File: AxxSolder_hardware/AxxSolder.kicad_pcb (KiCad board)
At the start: 2 copper layers, 39 x 82.5 mm, 138 parts, among them IC1 TLV76733DRVR, IC2 OPA2387DSGT, IC3 LMR54406DBVR, IC4 STM32G431CBT6, IC5 TPD4E1U06DBVR, IC6 STUSB4500QTR, IC7 MAX16171ATA_VY+T, IC8 LTC4440AHMS8E, IC9 INA281A5QDBVRQ1, J1 USB4110-GF-A, J2 691243110009, J3 TSW-102-07-T-S, J4 61300611821, J5 TSW-102-07-T-S, J6 TSW-102-07-T-S, Q1 STL9P3LLH6, Q2 STL10N3LLH5, Q3 2N7002NXAKR, U2 PEC11J-9215F-S0015, U3 BSC014N04LS

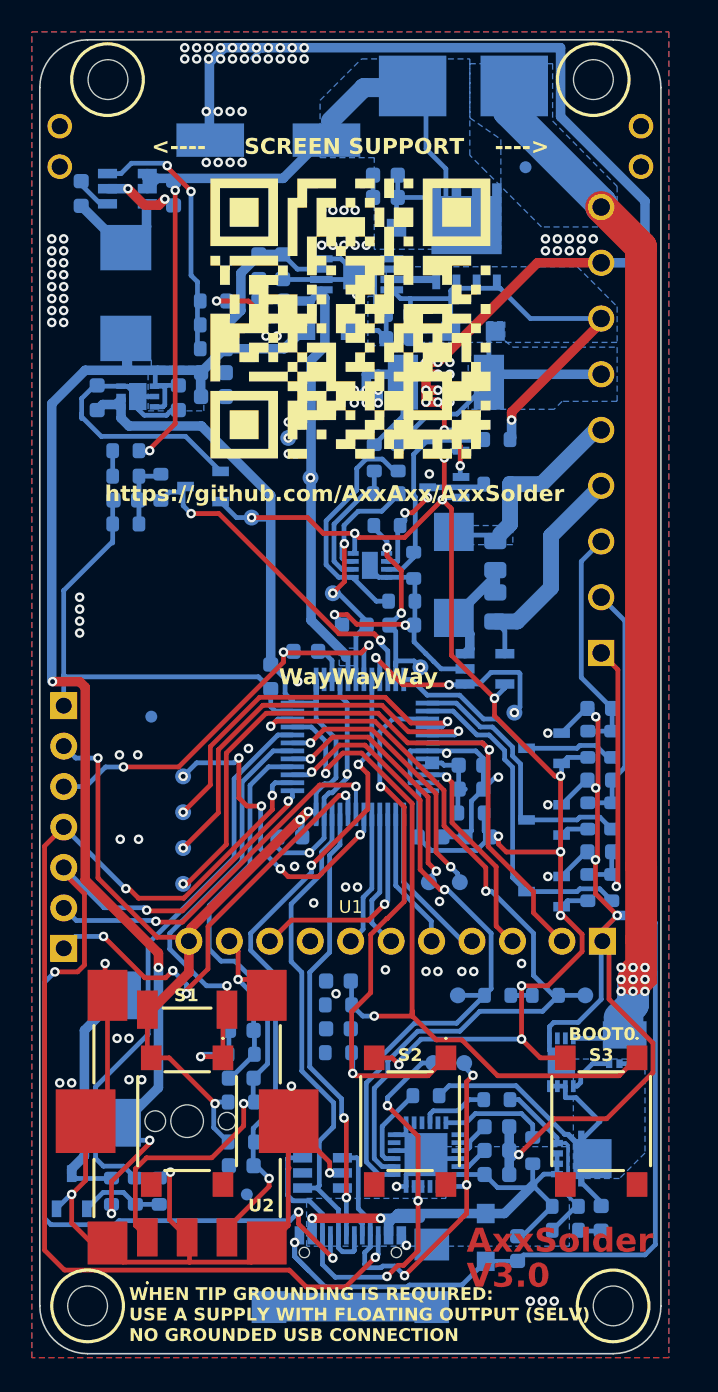
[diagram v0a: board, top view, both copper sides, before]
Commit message: Create Lite version of board
Mark all USB-C components as DNP (except I2C pullups)
Swap LCD footprint from Adafruit 4311 to commodity GMT020-02 LCD
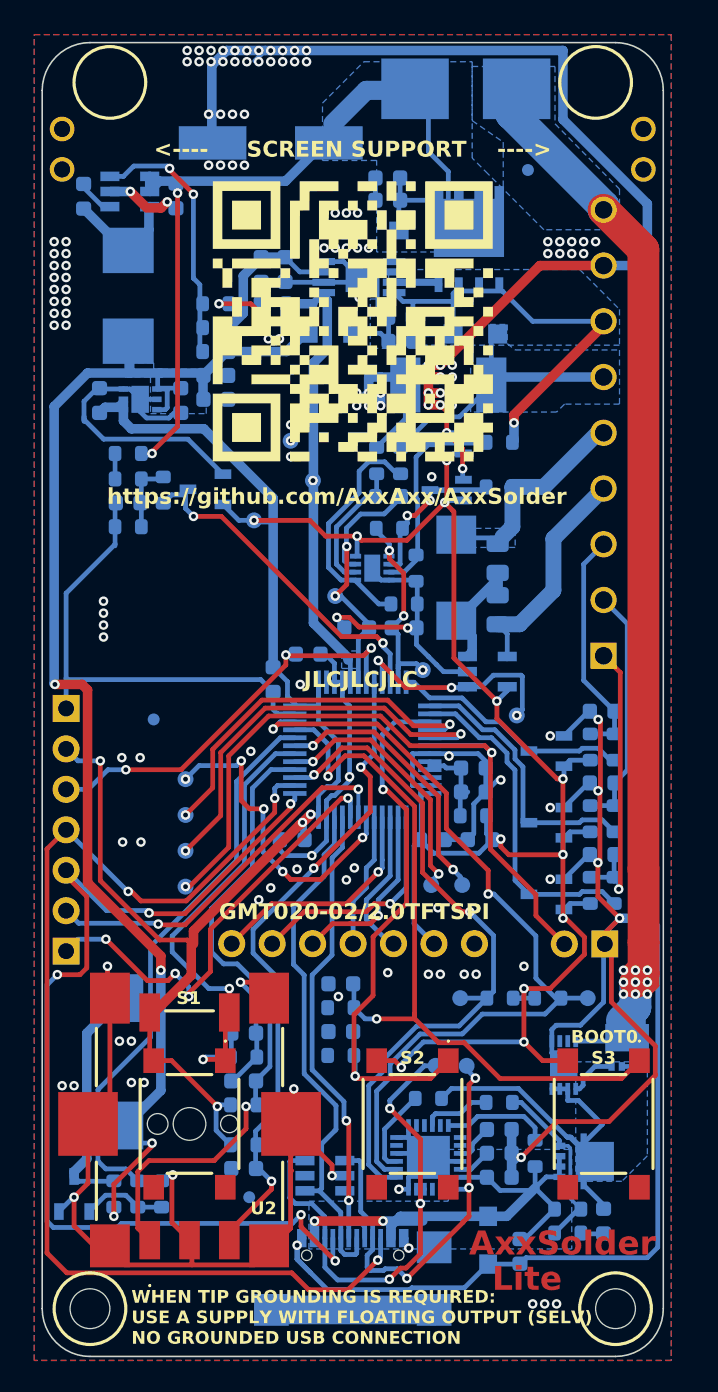
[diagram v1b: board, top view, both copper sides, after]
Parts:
- U1: footprint footprints:Adafruit_240x320_TFT -> Connector_PinHeader_2.54mm:PinHeader_1x07_P2.54mm_Vertical
- moved U1 7.84 mm to (173.1, 124.3), turned to 90 degrees
- moved C1 0.23 mm to (169.8, 90.1)
- moved C10 0.23 mm to (191.2, 143.6)
- moved C11 0.23 mm to (189.8, 138.9)
- moved C12 0.23 mm to (189.8, 137.4)
- moved C13 0.23 mm to (189.8, 135.9)
- moved C14 0.23 mm to (177.8, 106.1)
- moved C15 0.23 mm to (176.8, 117.7)
- moved C16 0.23 mm to (185.7, 117.7)
- moved C17 0.23 mm to (175.7, 107.7)
- moved C18 0.23 mm to (188.2, 113.2)
- moved C19 0.23 mm to (188.2, 114.7)
- moved C2 0.23 mm to (164.8, 90.1)
- moved C20 0.23 mm to (188.7, 117.7)
- moved C21 0.23 mm to (173.8, 129.9)
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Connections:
- C12 pad 1: Net-(IC6-VREG_2V7) -> Net-(C12-Pad1)
- C13 pad 1: Net-(IC6-VREG_1V2) -> Net-(C13-Pad1)
- IC4 pad 22: /SD_CS -> unconnected-(IC4-PB10-Pad22)
- R14 pad 1: Net-(IC6-VBUS_VS_DISCH) -> Net-(R14-Pad1)
- R15 pad 1: Net-(IC6-VBUS_EN_SNK) -> Net-(R15-Pad1)
- R17 pad 1: Net-(IC6-DISCH) -> Net-(R17-Pad1)
- U1 pad 2: +3.3V -> /SPI_DC
- U1 pad 3: GND -> /SPI_RST
- U1 pad 4: /SPI_SCK -> /SPI_MOSI
- U1 pad 5: unconnected-(U1-NC-Pad5) -> /SPI_SCK
- U1 pad 6: /SPI_MOSI -> +3.3V
- U1 pad 7: /SPI_CS -> GND
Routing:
- net /SD_CS: track 13.3 -> 0.00 mm, vias 1 -> 0
- net +3.3V: track 199.4 -> 207.2 mm
- net /SPI_CS: track 8.71 -> 14.9 mm, vias 0 -> 1
- net /SPI_SCK: track 13.9 -> 9.39 mm, vias 1 -> 0
- net /SPI_DC: track 10.1 -> 14.3 mm, vias 0 -> 1
- net GND: track 447.9 -> 445.6 mm, vias 149 -> 150
- net /SPI_RST: track 9.52 -> 11.6 mm, vias 0 -> 1
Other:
- board text added: "2024-05"
- board text added: "GMT020-02/2.0TFTSPI"
- board text added: "JLCJLCJLC"
- board text added: "Lite"
- board text added: "Lite V3.1"
- board text removed: "2024-02"
- board text removed: "V3.0"
- board text removed: "WayWayWay"

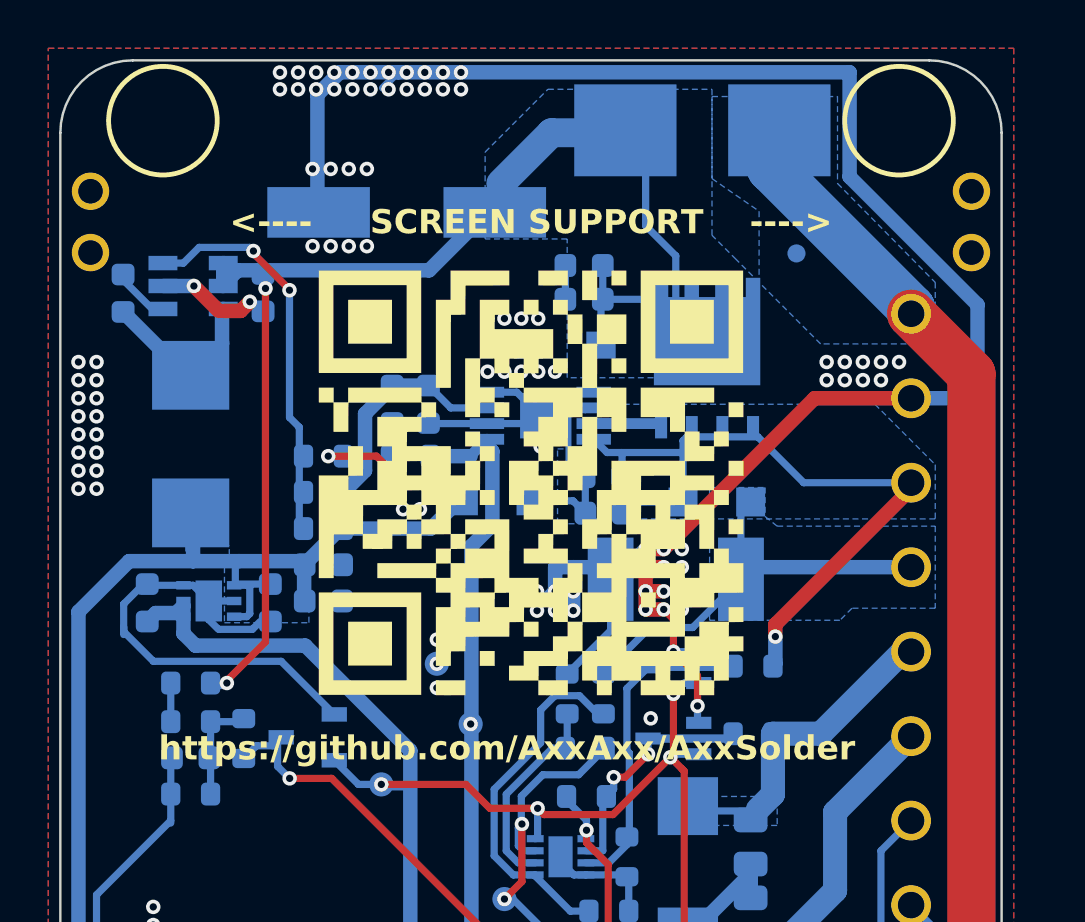
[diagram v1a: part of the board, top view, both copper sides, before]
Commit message: Finish Lite modifications
Fix upper mounting holes (no longer align with display; now aligned to PCB)
Add GitHub link for licensing purposes (I think this is necesssary for GPL)
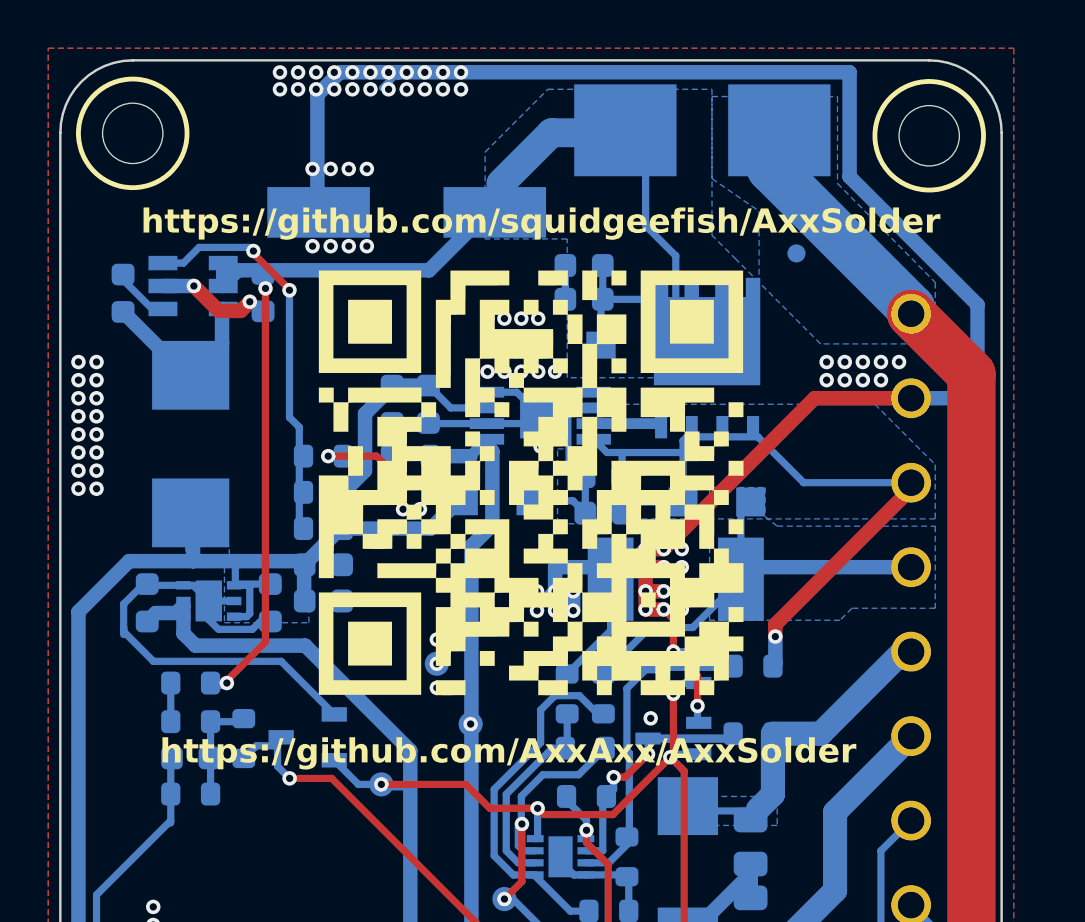
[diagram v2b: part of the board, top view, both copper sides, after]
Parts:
- removed J5, J6: TSW-102-07-T-S, footprints:TSW-102-XX-YY-S
- added H3: MountingHole, MountingHole:MountingHole_2.5mm, F.Cu at (164.2, 70.7)
- added H4: MountingHole, MountingHole:MountingHole_2.5mm, F.Cu at (197.2, 70.8)
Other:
- board text added: "Lite V3.0"
- board text added: "https://github.com/squidgeefish/AxxSolder"
- board text removed: "<---- SCREEN SUPPORT ---->"
- board text removed: "Lite V3.1"
